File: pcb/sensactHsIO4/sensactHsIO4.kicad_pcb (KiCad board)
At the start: 2 copper layers, 90 x 58.5 mm, 148 parts, among them J1 Bus, J2 PROG, J3 OUT0-3, J4 IN0-3 IO4-7, J5 IO8-15, J6 PSU+BUS, J7 L- L+ R- R+, Q1 IRLML6344, Q10 IRLML6344, Q11 IRLML6344, Q12 IRLML6344, Q2 IRLML6344, Q3 IRLML6344, Q4 IRLML6344, Q5 IRLML6344, Q6 IRLML6344, Q7 IRLML6344, Q8 IRLML6344, Q9 IRLML6344, SW1 BOOT, SW2 TERM OFF ON, U1 ESP32-WROOM-32U, U10 SRV05, U11 SRV05, U12 SRV05, U13 MAX98357AETE+T, U14 MAX98357AETE+T, U2 SN65HVD230, U3 MAX3485, U4 CPC1018N, U5 CPC1018N, U6 CPC1018N, U7 CPC1018N, U8 LMR14206, U9 SRV05

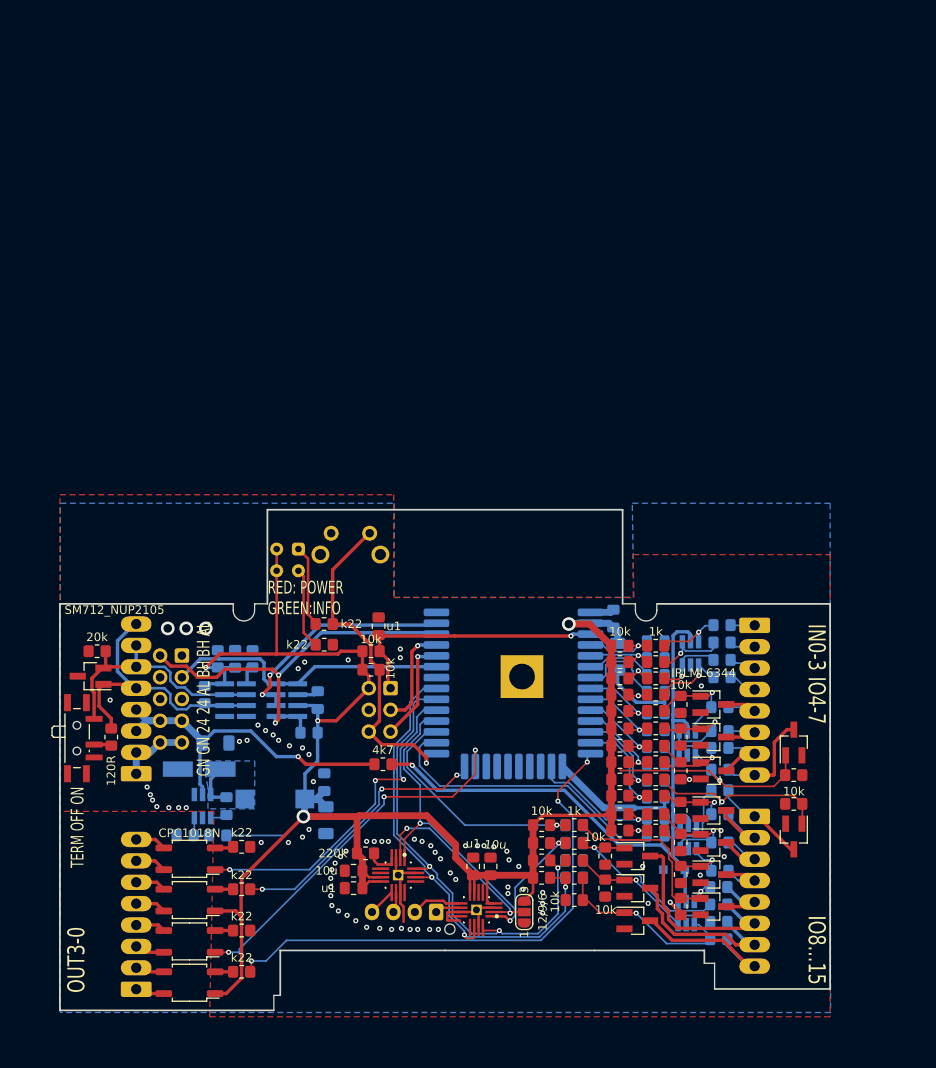
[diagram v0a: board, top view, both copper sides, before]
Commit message: Improvements in pcb design of sensactOutdoor and sensactHsIO4
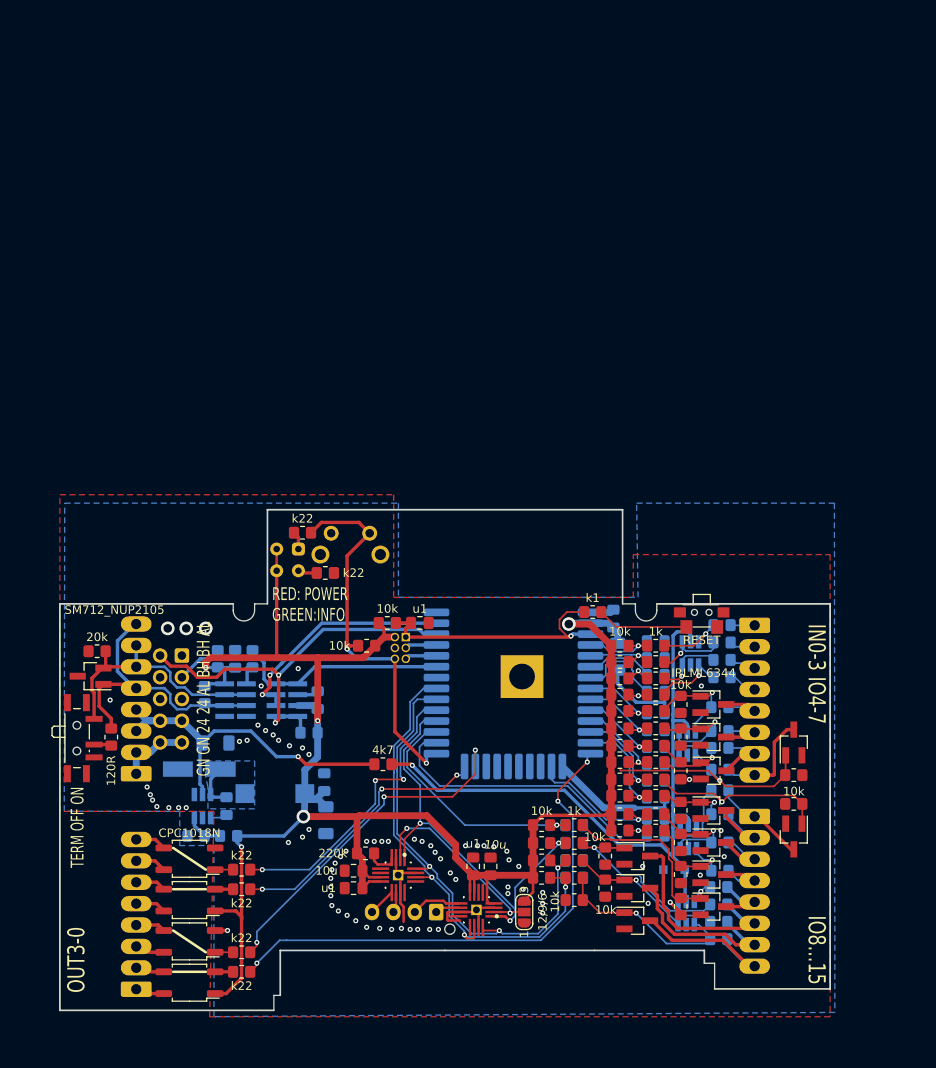
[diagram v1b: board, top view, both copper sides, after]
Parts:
- added R79: k1, Resistor_SMD:R_0805_2012Metric_Pad1.20x1.40mm_HandSolder, F.Cu at (167.3, 108.7)
- added SW3: RESET, sensact:SW_SPST_2x4x3,5, F.Cu at (180.0, 108.8)
- J2: footprint Connector_IDC:IDC-Header_2x03_P2.54mm_Vertical -> liebler_CONN:IDC_2x03_P1.27mm_Vertical
- moved R3 11.0 mm to (133.3, 99.4)
- moved R77 8.38 mm to (136.0, 104.1)
- moved C1 4.84 mm to (147.1, 110.0), turned to 180 degrees
- moved J2 4.84 mm to (144.8, 112.9)
- moved R1 3.81 mm to (143.3, 110.0)
- moved R2 2.84 mm to (140.8, 112.6), turned to 0 degrees
- moved R8 2.67 mm to (126.2, 138.8)
- moved R6 2.54 mm to (126.2, 148.5)
- moved R10 1.27 mm to (120.9, 134.9)
- moved R9 1.27 mm to (124.7, 134.9)
- moved L1 0.64 mm to (130.1, 129.9)
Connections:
- R6 pad 1: GND -> OUT2
- R8 pad 1: GND -> OUT0
- U5 pad 1: OUT2 -> Net-(R6-Pad2)
- U5 pad 2: Net-(R6-Pad2) -> GND
- U7 pad 1: OUT0 -> Net-(R8-Pad2)
- U7 pad 2: Net-(R8-Pad2) -> GND
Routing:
- net Net-(R79-Pad1): track 0.00 -> 10.7 mm
- net PROG_RX: track 12.3 -> 3.73 mm, vias 1 -> 0
- net PROG_TX: track 12.0 -> 3.73 mm, vias 1 -> 0
- net Net-(D1-Pad1): track 9.59 -> 2.12 mm
- net Net-(D1-Pad3): track 9.47 -> 2.25 mm
- net PROG_IO0: track 39.8 -> 46.0 mm, vias 1 -> 2
- net OUT0: track 38.8 -> 34.7 mm
- net OUT2: track 44.5 -> 41.1 mm
- net +3V3: track 218.5 -> 217.0 mm, vias 4 -> 5
- net GND: track 70.1 -> 71.6 mm, vias 81 -> 77
- net /psu/FB: track 3.92 -> 4.44 mm
- net OUT3: track 61.8 -> 61.3 mm

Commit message: various changes
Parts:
- added C30: 1u, Capacitor_SMD:C_1206_3216Metric_Pad1.33x1.80mm_HandSolder, F.Cu at (120.8, 124.0)
- added C31: 1u, Capacitor_SMD:C_0805_2012Metric_Pad1.18x1.45mm_HandSolder, F.Cu at (139.4, 135.9)
- added J11: BUS, Connector_Phoenix_MC:PhoenixContact_MC_1,5_4-G-3.5_1x04_P3.50mm_Horizontal, B.Cu at (113.0, 120.8)
- added J12: 24V, Connector_Phoenix_MC:PhoenixContact_MC_1,5_2-G-3.5_1x02_P3.50mm_Horizontal, B.Cu at (113.0, 130.0)
- added R80: 4k7, Resistor_SMD:R_0805_2012Metric_Pad1.20x1.40mm_HandSolder, F.Cu at (149.4, 132.8)
- added R81: 4k7, Resistor_SMD:R_0805_2012Metric_Pad1.20x1.40mm_HandSolder, F.Cu at (137.5, 140.8)
- added R82: 4k7, Resistor_SMD:R_0805_2012Metric_Pad1.20x1.40mm_HandSolder, F.Cu at (135.5, 140.8)
- added R83: 4k7, Resistor_SMD:R_0805_2012Metric_Pad1.20x1.40mm_HandSolder, F.Cu at (133.5, 140.8)
- added R84: 4k7, Resistor_SMD:R_0805_2012Metric_Pad1.20x1.40mm_HandSolder, F.Cu at (131.4, 140.8)
- added R85: 2k2, Resistor_SMD:R_0805_2012Metric_Pad1.20x1.40mm_HandSolder, F.Cu at (139.6, 140.8)
- added R86: 2k2, Resistor_SMD:R_0805_2012Metric_Pad1.20x1.40mm_HandSolder, F.Cu at (139.3, 137.9)
- added R87: 2k2, Resistor_SMD:R_0805_2012Metric_Pad1.20x1.40mm_HandSolder, F.Cu at (130.4, 137.0)
- added R88: 2k2, Resistor_SMD:R_0805_2012Metric_Pad1.20x1.40mm_HandSolder, F.Cu at (129.4, 140.8)
- added SW4: INT0, liebler_MECH:SS12D00, B.Cu at (135.5, 107.1)
- added SW5: INT1, liebler_MECH:SS12D00, B.Cu at (135.5, 121.0)
- added SW6: INT2, liebler_MECH:SS12D00, B.Cu at (135.5, 117.3)
- C4: value u1 -> 10u; footprint Capacitor_SMD:C_0805_2012Metric_Pad1.18x1.45mm_HandSolder -> Capacitor_SMD:C_1206_3216Metric_Pad1.33x1.80mm_HandSolder
- D3: value SM712_NUP2105 -> NUP2105
- J6: value PSU+BUS -> AIN; footprint liebler_CONN:PhoenixContact_MC_0,5_8-G-2.5_1x08_P2.50mm_Horizontal -> Connector_JST:JST_XH_B4B-XH-AM_1x04_P2.50mm_Vertical
- R4: value 10k -> isI2C; footprint Resistor_SMD:R_0805_2012Metric_Pad1.20x1.40mm_HandSolder -> Resistor_SMD:R_1206_3216Metric_Pad1.30x1.75mm_HandSolder
- R71: value 20k -> isI2C; footprint Resistor_SMD:R_0805_2012Metric_Pad1.20x1.40mm_HandSolder -> Resistor_SMD:R_1206_3216Metric_Pad1.30x1.75mm_HandSolder; moved to B.Cu
- R72: value 20k -> 4k7; moved to F.Cu
- R75, R76: footprint Resistor_SMD:R_0805_2012Metric_Pad1.20x1.40mm_HandSolder -> Resistor_SMD:R_1206_3216Metric_Pad1.30x1.75mm_HandSolder
- U2: value SN65HVD230 -> ISO1050DUB; footprint sensact:SOIC-8_3.9x4.9mm_Pitch1.27mm_handsolder -> liebler_SEMICONDUCTORS:SOP-8_6.62x9.15mm_P2.54mm_handsolder
- U3: value MAX3485 -> ADS1115IDGS; footprint sensact:SOIC-8_3.9x4.9mm_Pitch1.27mm_handsolder -> Package_SO:TSSOP-10_3x3mm_P0.5mm; moved to F.Cu
- moved J6 29.1 mm to (138.2, 143.8), turned to 180 degrees
- moved R71 26.4 mm to (135.8, 113.4), turned to 0 degrees
- moved R72 23.2 mm to (140.8, 131.8)
- moved U3 19.4 mm to (134.5, 137.0), turned to 0 degrees
- moved R74 19.4 mm to (123.8, 122.4)
- moved R76 19.3 mm to (119.0, 110.7), turned to 90 degrees
- moved R10 18.8 mm to (139.4, 131.6), turned to 0 degrees
- moved C5 18.0 mm to (141.7, 106.4), turned to 0 degrees
- moved R9 15.7 mm to (139.4, 129.5), turned to 0 degrees
- moved U2 9.09 mm to (135.8, 112.1)
- moved R4 8.89 mm to (135.8, 110.9), turned to 0 degrees
- moved C4 8.75 mm to (128.4, 113.4), turned to 270 degrees
- moved C8 8.30 mm to (140.5, 126.0), turned to 90 degrees
- moved R75 7.67 mm to (116.6, 110.7), turned to 90 degrees
- moved R2 6.53 mm to (143.5, 118.6), turned to 180 degrees
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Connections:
- C4 pad 1: +3V3 -> +5VA
- C4 pad 2: GND -> GNDA
- D3 pad 1: RS485_A -> CANL
- D3 pad 2: RS485_B -> CANH
- D3 pad 3: GND -> GNDA
- J1 pad 2: SCL -> CANH
- J1 pad 3: SDA -> CANL
- J1 pad 4: Net-(J1-Pad4) -> +5VA
- J1 pad 6: Net-(J1-Pad6) -> GNDA
- J6 pad 1: GND -> Net-(J6-Pad1)
- J6 pad 2: GND -> Net-(J6-Pad2)
- J6 pad 3: +24V -> Net-(J6-Pad3)
- J6 pad 4: +24V -> Net-(J6-Pad4)
- R4 pad 1: GND -> CANH
- R4 pad 2: Net-(R4-Pad2) -> CANR
- R71 pad 1: RS485_B -> CANL
- R71 pad 2: GND -> CANT
- R72 pad 1: +3V3 -> IO15
- R72 pad 2: RS485_A -> +3V3
- R73 pad 1: RS485_A -> CANH
- R75 pad 1: SDA -> CANH
- R76 pad 1: SCL -> CANL
- SW2 pad 1: RS485_B -> CANL
- U1 pad 33: SDA -> CANT
- U1 pad 36: SCL -> CANR
- U1 pad 37: DE_RE -> IRQ
- U2 pad 1: SDA -> +3V3
- U2 pad 2: GND -> CANR
- U2 pad 3: +3V3 -> CANT
- U2 pad 4: SCL -> GND
- U2 pad 5: Net-(U2-Pad5) -> GNDA
- U2 pad 6: RS485_A -> CANL
- U2 pad 7: RS485_B -> CANH
- U2 pad 8: Net-(R4-Pad2) -> +5VA
- U3 pad 1: SDA -> GND
- U3 pad 2: DE_RE -> Net-(U3-Pad2)
- U3 pad 3: DE_RE -> GND
- U3 pad 4: SCL -> Net-(R83-Pad2)
- U3 pad 5: GND -> Net-(R84-Pad2)
- U3 pad 6: RS485_A -> Net-(R81-Pad2)
- U3 pad 7: RS485_B -> Net-(R82-Pad2)
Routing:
- net CANH: track 0.00 -> 52.4 mm
- net SCL: track 50.3 -> 0.00 mm, vias 2 -> 0
- net CANL: track 0.00 -> 41.9 mm, vias 0 -> 1
- net RS485_A: track 36.6 -> 0.00 mm
- net SDA: track 34.9 -> 0.00 mm
- net GNDA: track 0.00 -> 32.4 mm
- net +5VA: track 0.00 -> 30.4 mm
- net RS485_B: track 30.0 -> 0.00 mm
- net DE_RE: track 27.7 -> 0.00 mm, vias 2 -> 0
- net IRQ: track 0.00 -> 27.0 mm
- net 3V3_ZDIODE: track 77.9 -> 98.9 mm
- net +3V3: track 217.0 -> 237.9 mm
- net Net-(J1-Pad5): track 0.00 -> 17.4 mm
- net /psu/FB: track 4.44 -> 21.8 mm
- net IO15: track 62.0 -> 78.5 mm, vias 3 -> 6
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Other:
- rule pad_to_mask_clearance: 0.05 -> 0
- board text added: "CH CL CL CH"
- board text added: "GN 24"
- board text removed: "GN GN 24 24 AL BH BH AL"

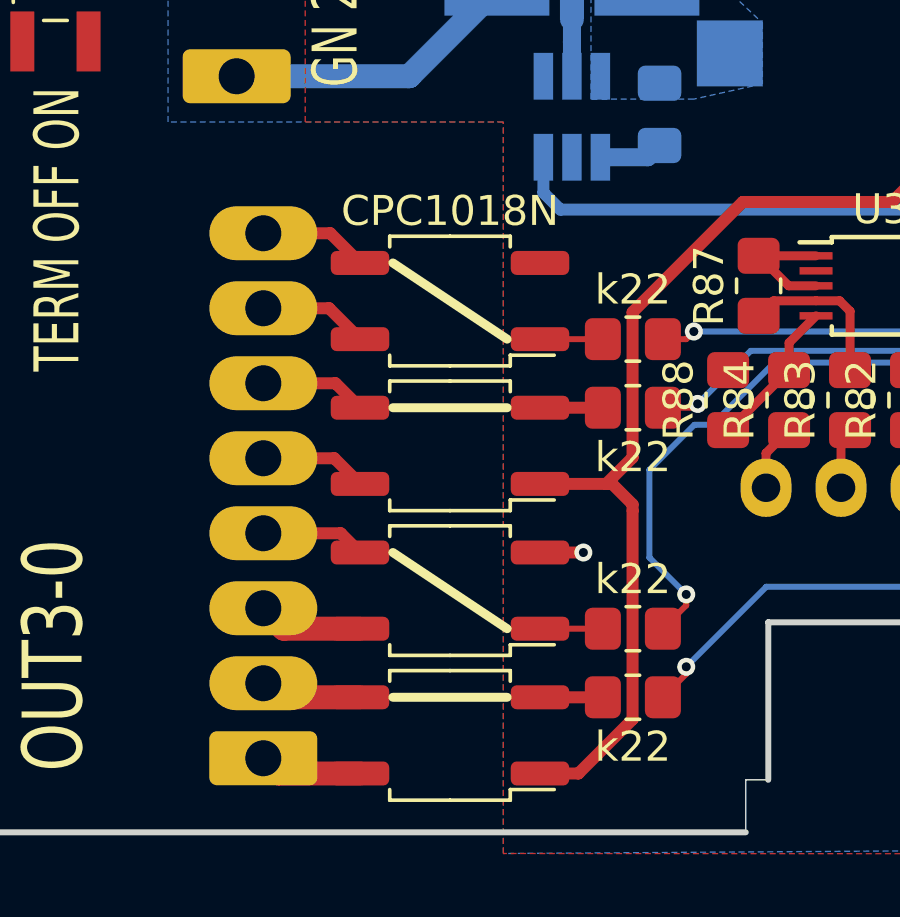
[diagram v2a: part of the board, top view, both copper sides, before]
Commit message: Renamed liebler_IC to liebler_SEMICONDUCTORS
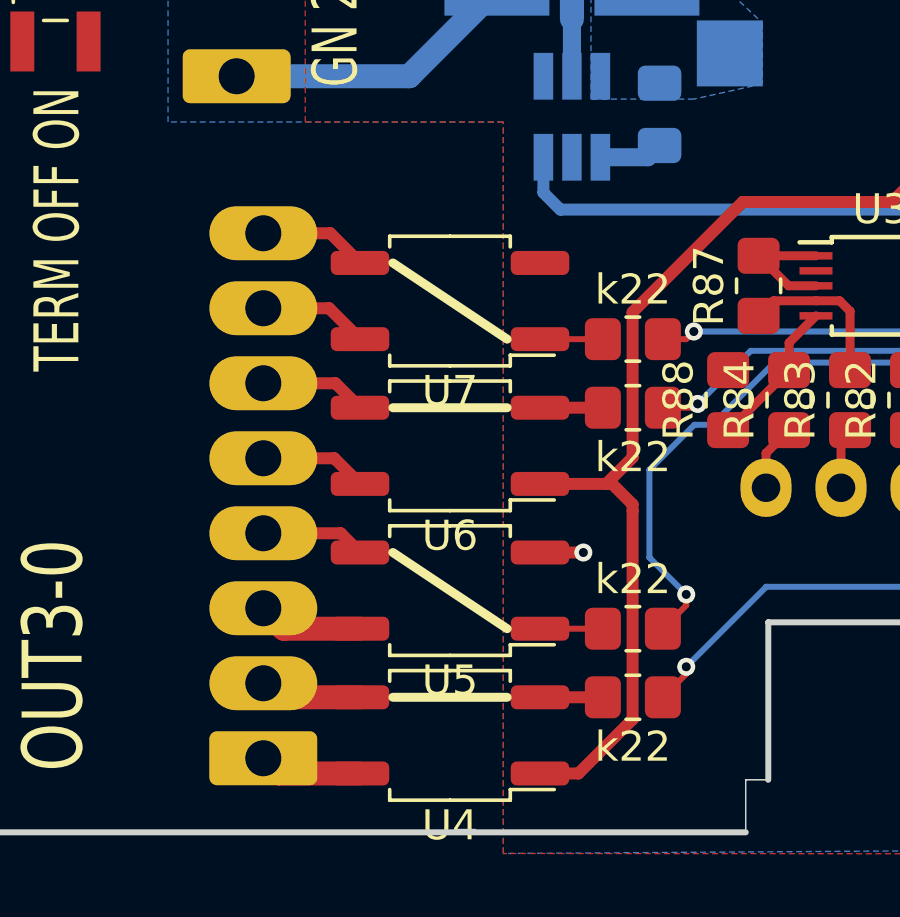
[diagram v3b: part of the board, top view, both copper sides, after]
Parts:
- U4, U5, U6, U7: footprint liebler_IC:SOP-4_3.8x4.1mm_P2.54mm_handsolder -> liebler_SEMICONDUCTORS:SOP-4_3.8x4.1mm_P2.54mm_handsolder

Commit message: PCB optimizations
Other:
- outline, holes or cut-outs redrawn

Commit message: Various
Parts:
- removed C28: 10u, Capacitor_SMD:C_0805_2012Metric_Pad1.18x1.45mm_HandSolder
- removed C29: u1, Capacitor_SMD:C_0805_2012Metric_Pad1.18x1.45mm_HandSolder
- removed C30: 1u, Capacitor_SMD:C_1206_3216Metric_Pad1.33x1.80mm_HandSolder
- removed C31: 1u, Capacitor_SMD:C_0805_2012Metric_Pad1.18x1.45mm_HandSolder
- removed J11: BUS, Connector_Phoenix_MC:PhoenixContact_MC_1,5_4-G-3.5_1x04_P3.50mm_Horizontal
- removed J12: 24V, Connector_Phoenix_MC:PhoenixContact_MC_1,5_2-G-3.5_1x02_P3.50mm_Horizontal
- removed Q10, Q11, Q12, Q3, Q4, Q5, Q6, Q7, Q8, Q9: IRLML6344, Package_TO_SOT_SMD:SOT-23_Handsoldering
- removed R80, R81, R82, R83, R84: 4k7, Resistor_SMD:R_0805_2012Metric_Pad1.20x1.40mm_HandSolder
- removed R85, R86, R87, R88: 2k2, Resistor_SMD:R_0805_2012Metric_Pad1.20x1.40mm_HandSolder
- removed SW1: BOOT, Button_Switch_THT:SW_Tactile_SPST_Angled_PTS645Vx58-2LFS
- added BZ1: Buzzer, liebler_MECH:XDCR_CMT-7525-80-SMT-TR, B.Cu at (137.5, 85.4)
- added D5: NUP2105L, Package_TO_SOT_SMD:SOT-23_Handsoldering, B.Cu at (181.8, 138.6)
- added H1: MountingHole, MountingHole:MountingHole_2mm, F.Cu at (169.0, 43.4)
- added H2: MountingHole, MountingHole:MountingHole_2mm, F.Cu at (159.5, 58.5)
- added J8: Conn_01x10, Connector_FFC-FPC:Hirose_FH12-10S-0.5SH_1x10-1MP_P0.50mm_Horizontal, B.Cu at (147.8, 86.8)
- added J9: AOUT, Connector_JST:JST_XH_B4B-XH-A_1x04_P2.50mm_Vertical, B.Cu at (151.5, 137.7)
- added JP10: OUT_IN0, Jumper:SolderJumper-3_P1.3mm_Open_RoundedPad1.0x1.5mm, F.Cu at (118.3, 120.4)
- added JP11: OUT_IN0, Jumper:SolderJumper-3_P1.3mm_Open_RoundedPad1.0x1.5mm, F.Cu at (118.3, 126.6)
- added JP12: OUT_IN0, Jumper:SolderJumper-3_P1.3mm_Open_RoundedPad1.0x1.5mm, F.Cu at (118.3, 134.4)
- added JP13: OUT_IN0, Jumper:SolderJumper-3_P1.3mm_Open_RoundedPad1.0x1.5mm, F.Cu at (122.9, 114.2)
- added JP14: OUT_IN0, Jumper:SolderJumper-3_P1.3mm_Open_RoundedPad1.0x1.5mm, F.Cu at (122.9, 120.4)
- added JP15: OUT_IN0, Jumper:SolderJumper-3_P1.3mm_Open_RoundedPad1.0x1.5mm, F.Cu at (122.9, 126.6)
- added JP16: OUT_IN0, Jumper:SolderJumper-3_P1.3mm_Open_RoundedPad1.0x1.5mm, F.Cu at (122.9, 134.4)
- added JP17: OUT_IN0, Jumper:SolderJumper-3_P1.3mm_Open_RoundedPad1.0x1.5mm, F.Cu at (118.3, 137.5)
- added JP18: OUT_IN0, Jumper:SolderJumper-3_P1.3mm_Open_RoundedPad1.0x1.5mm, F.Cu at (118.3, 143.7)
- added JP19: OUT_IN0, Jumper:SolderJumper-3_P1.3mm_Open_RoundedPad1.0x1.5mm, F.Cu at (118.3, 149.9)
- added JP2: OUT_IN0, Jumper:SolderJumper-3_P1.3mm_Open_RoundedPad1.0x1.5mm, F.Cu at (118.3, 117.3)
- added JP20: OUT_IN0, Jumper:SolderJumper-3_P1.3mm_Open_RoundedPad1.0x1.5mm, F.Cu at (122.9, 137.5)
- added JP21: OUT_IN0, Jumper:SolderJumper-3_P1.3mm_Open_RoundedPad1.0x1.5mm, F.Cu at (122.9, 143.7)
- added JP22: OUT_IN0, Jumper:SolderJumper-3_P1.3mm_Open_RoundedPad1.0x1.5mm, F.Cu at (122.9, 149.9)
- added JP23: OUT_IN0, Jumper:SolderJumper-3_P1.3mm_Open_RoundedPad1.0x1.5mm, F.Cu at (118.3, 140.6)
- added JP24: OUT_IN0, Jumper:SolderJumper-3_P1.3mm_Open_RoundedPad1.0x1.5mm, F.Cu at (118.3, 146.8)
- added JP25: OUT_IN0, Jumper:SolderJumper-3_P1.3mm_Open_RoundedPad1.0x1.5mm, F.Cu at (118.3, 153.0)
- added JP26: OUT_IN0, Jumper:SolderJumper-3_P1.3mm_Open_RoundedPad1.0x1.5mm, F.Cu at (122.9, 140.6)
- added JP27: OUT_IN0, Jumper:SolderJumper-3_P1.3mm_Open_RoundedPad1.0x1.5mm, F.Cu at (122.9, 146.8)
- added JP28: OUT_IN0, Jumper:SolderJumper-3_P1.3mm_Open_RoundedPad1.0x1.5mm, F.Cu at (123.0, 152.9)
- added JP29: SCL, Jumper:SolderJumper-2_P1.3mm_Open_RoundedPad1.0x1.5mm, F.Cu at (169.7, 126.8)
- added JP3: OUT_IN0, Jumper:SolderJumper-3_P1.3mm_Open_RoundedPad1.0x1.5mm, F.Cu at (118.3, 123.5)
- added JP30: SDA, Jumper:SolderJumper-2_P1.3mm_Open_RoundedPad1.0x1.5mm, F.Cu at (169.7, 124.2)
- added JP31: IO12, Jumper:SolderJumper-3_P1.3mm_Open_RoundedPad1.0x1.5mm, F.Cu at (163.4, 128.1)
- added JP32: BUST, Jumper:SolderJumper-3_P1.3mm_Open_RoundedPad1.0x1.5mm, F.Cu at (166.8, 140.6)
- added JP33: BUSR, Jumper:SolderJumper-3_P1.3mm_Open_RoundedPad1.0x1.5mm, F.Cu at (166.8, 136.8)
- added JP34: BUST, Jumper:SolderJumper-3_P1.3mm_Open_RoundedPad1.0x1.5mm, F.Cu at (183.5, 143.6)
- added JP35: BUSR, Jumper:SolderJumper-3_P1.3mm_Open_RoundedPad1.0x1.5mm, F.Cu at (183.5, 138.8)
- added JP4: OUT_IN0, Jumper:SolderJumper-3_P1.3mm_Open_RoundedPad1.0x1.5mm, F.Cu at (118.3, 129.7)
- added JP5: OUT_IN0, Jumper:SolderJumper-3_P1.3mm_Open_RoundedPad1.0x1.5mm, F.Cu at (122.9, 111.1)
- added JP6: OUT_IN0, Jumper:SolderJumper-3_P1.3mm_Open_RoundedPad1.0x1.5mm, F.Cu at (122.9, 117.3)
- added JP7: OUT_IN0, Jumper:SolderJumper-3_P1.3mm_Open_RoundedPad1.0x1.5mm, F.Cu at (122.9, 123.5)
- added JP8: OUT_IN0, Jumper:SolderJumper-3_P1.3mm_Open_RoundedPad1.0x1.5mm, F.Cu at (122.9, 129.7)
- added JP9: OUT_IN0, Jumper:SolderJumper-3_P1.3mm_Open_RoundedPad1.0x1.5mm, F.Cu at (118.3, 114.2)
- added U15: SRV05-4, liebler_SEMICONDUCTORS:SOT-23-6-spezial, B.Cu at (149.4, 132.8)
- added U16: SRV05-4, liebler_SEMICONDUCTORS:SOT-23-6-spezial, B.Cu at (158.9, 132.8)
- added X1: LH114, liebler_OPTO:FP-114 13pol, F.Cu at (149.0, 90.0)
- C1, C27: footprint Capacitor_SMD:C_0805_2012Metric_Pad1.18x1.45mm_HandSolder -> Capacitor_SMD:C_0402_1005Metric; moved to B.Cu
- C10, C11, C12, C13, C14, C15, C16, C17, C18, C19, C2, C20, C22, C7, C9: footprint Capacitor_SMD:C_0805_2012Metric_Pad1.18x1.45mm_HandSolder -> Capacitor_SMD:C_0603_1608Metric
- C21: value u1 -> 10u; footprint Capacitor_SMD:C_0805_2012Metric_Pad1.18x1.45mm_HandSolder -> Capacitor_SMD:C_1206_3216Metric
- C23: value u1 -> 10n; footprint Capacitor_SMD:C_0805_2012Metric_Pad1.18x1.45mm_HandSolder -> Capacitor_SMD:C_0603_1608Metric
- C24: value u1 -> 22u; footprint Capacitor_SMD:C_0805_2012Metric_Pad1.18x1.45mm_HandSolder -> Capacitor_SMD:C_0603_1608Metric
- C25, C5: footprint Capacitor_SMD:C_0805_2012Metric_Pad1.18x1.45mm_HandSolder -> Capacitor_SMD:C_0402_1005Metric
- C26: value 10u -> 1u; footprint Capacitor_SMD:C_0805_2012Metric_Pad1.18x1.45mm_HandSolder -> Capacitor_SMD:C_0402_1005Metric; moved to B.Cu
- C3: value 22u -> u1; footprint Capacitor_SMD:C_1206_3216Metric_Pad1.33x1.80mm_HandSolder -> Capacitor_SMD:C_0603_1608Metric
- C4: value 10u -> u1; footprint Capacitor_SMD:C_1206_3216Metric_Pad1.33x1.80mm_HandSolder -> Capacitor_SMD:C_0402_1005Metric
- C6: value 4u7 -> 22u; footprint Capacitor_SMD:C_1206_3216Metric_Pad1.33x1.80mm_HandSolder -> Capacitor_SMD:C_0603_1608Metric
- C8: value m1 -> u1; footprint Capacitor_SMD:C_1206_3216Metric_Pad1.33x1.80mm_HandSolder -> Capacitor_SMD:C_0603_1608Metric
- D1: value R_POWER_G_INFO -> SM712; footprint liebler_SEMICONDUCTORS:Dialight-5530123F-0 -> Package_TO_SOT_SMD:SOT-23_Handsoldering
- D2: value MBR0540 -> D; footprint Diode_SMD:D_SMA_Handsoldering -> Diode_SMD:D_SOD-123
- D3: value NUP2105 -> 3V; footprint Package_TO_SOT_SMD:SOT-23_Handsoldering -> Diode_SMD:D_SOD-123; moved to B.Cu
- D4: value 3V -> SS34; footprint Diode_SMD:D_SOD-323_HandSoldering -> Diode_SMD:D_SMA
- J1: value Bus -> BUS; footprint Connector_IDC:IDC-Header_2x05_P2.54mm_Horizontal -> Connector_Phoenix_MC:PhoenixContact_MC_1,5_4-G-3.5_1x04_P3.50mm_Horizontal
- J2: value PROG -> Bus; footprint liebler_CONN:IDC_2x03_P1.27mm_Vertical -> Connector_IDC:IDC-Header_2x05_P2.54mm_Horizontal
- J3: value OUT0-3 -> 24V; footprint liebler_CONN:PhoenixContact_MC_0,5_8-G-2.5_1x08_P2.50mm_Horizontal -> Connector_Phoenix_MC:PhoenixContact_MC_1,5_2-G-3.5_1x02_P3.50mm_Horizontal
- J4: value IN0-3 IO4-7 -> PROG; footprint liebler_CONN:PhoenixContact_MC_0,5_8-G-2.5_1x08_P2.50mm_Horizontal -> liebler_CONN:IDC_2x03_P1.27mm_Vertical
- J5: value IO8-15 -> IN0-3 IO4-7
- J6: value AIN -> IO8-15; footprint Connector_JST:JST_XH_B4B-XH-AM_1x04_P2.50mm_Vertical -> liebler_CONN:PhoenixContact_MC_0,5_8-G-2.5_1x08_P2.50mm_Horizontal
- J7: value L- L+ R- R+ -> HMI; footprint Connector_JST:JST_XH_B4B-XH-AM_1x04_P2.50mm_Vertical -> Connector_FFC-FPC:Hirose_FH12-10S-0.5SH_1x10-1MP_P0.50mm_Horizontal
- JP1: value 12/9/6 -> OUT_IN0; footprint Jumper:SolderJumper-3_P1.3mm_Open_RoundedPad1.0x1.5mm_NumberLabels -> Jumper:SolderJumper-3_P1.3mm_Open_RoundedPad1.0x1.5mm
- L1: value 33u -> 6u8; footprint sensact:L_7.3x7.3_H4.5_handsolder -> Inductor_SMD:L_Abracon_ASPI-0630LR
- Q1, Q2: value IRLML6344 -> AO3400A; footprint Package_TO_SOT_SMD:SOT-23_Handsoldering -> Package_TO_SOT_SMD:SOT-23; moved to B.Cu
- R1, R19, R28, R29, R30: value 10k -> k1; footprint Resistor_SMD:R_0805_2012Metric_Pad1.20x1.40mm_HandSolder -> Resistor_SMD:R_0603_1608Metric; moved to B.Cu
- R10: value 1k -> 10k; footprint Resistor_SMD:R_0805_2012Metric_Pad1.20x1.40mm_HandSolder -> Resistor_SMD:R_0402_1005Metric
- R11: value 10R -> 4k7; footprint Resistor_SMD:R_0805_2012Metric_Pad1.20x1.40mm_HandSolder -> Resistor_SMD:R_0603_1608Metric
- R12, R13, R14, R24, R25, R26: footprint Resistor_SMD:R_0805_2012Metric_Pad1.20x1.40mm_HandSolder -> Resistor_SMD:R_0603_1608Metric
- R15, R47, R66: value 1k -> 10R; footprint Resistor_SMD:R_0805_2012Metric_Pad1.20x1.40mm_HandSolder -> Resistor_SMD:R_0603_1608Metric; moved to B.Cu
- R16, R17, R18, R31, R48, R49, R50: value 1k -> k1; footprint Resistor_SMD:R_0805_2012Metric_Pad1.20x1.40mm_HandSolder -> Resistor_SMD:R_0603_1608Metric; moved to B.Cu
- R2, R20, R21, R22, R35, R43, R44, R51, R52, R53: footprint Resistor_SMD:R_0805_2012Metric_Pad1.20x1.40mm_HandSolder -> Resistor_SMD:R_0603_1608Metric; moved to B.Cu
- R23, R42: value 10R -> 10k; footprint Resistor_SMD:R_0805_2012Metric_Pad1.20x1.40mm_HandSolder -> Resistor_SMD:R_0603_1608Metric
- R27, R36, R37, R38, R45, R46, R67, R68, R69, R70: value 10k -> 10R; footprint Resistor_SMD:R_0805_2012Metric_Pad1.20x1.40mm_HandSolder -> Resistor_SMD:R_0603_1608Metric; moved to B.Cu
- R3: value k22 -> 10k; footprint Resistor_SMD:R_0805_2012Metric_Pad1.20x1.40mm_HandSolder -> Resistor_SMD:R_0603_1608Metric; moved to B.Cu
- R32, R33, R34: value 1k -> 10k; footprint Resistor_SMD:R_0805_2012Metric_Pad1.20x1.40mm_HandSolder -> Resistor_SMD:R_0603_1608Metric; moved to B.Cu
- R39, R40, R41: value 10R -> k1; footprint Resistor_SMD:R_0805_2012Metric_Pad1.20x1.40mm_HandSolder -> Resistor_SMD:R_0603_1608Metric
- R4: value isI2C -> 1k; footprint Resistor_SMD:R_1206_3216Metric_Pad1.30x1.75mm_HandSolder -> Resistor_SMD:R_0402_1005Metric
- R5, R6: value k22 -> 1k; footprint Resistor_SMD:R_0805_2012Metric_Pad1.20x1.40mm_HandSolder -> Resistor_SMD:R_0603_1608Metric; moved to B.Cu
- R54: value 10k -> 75k; footprint Resistor_SMD:R_0805_2012Metric_Pad1.20x1.40mm_HandSolder -> Resistor_SMD:R_0603_1608Metric; moved to B.Cu
- R55: value 10R -> 24K; footprint Resistor_SMD:R_0805_2012Metric_Pad1.20x1.40mm_HandSolder -> Resistor_SMD:R_0603_1608Metric
- R56, R58: value 10R -> 1k; footprint Resistor_SMD:R_0805_2012Metric_Pad1.20x1.40mm_HandSolder -> Resistor_SMD:R_0402_1005Metric
- R57: value 10R -> 1k; footprint Resistor_SMD:R_0805_2012Metric_Pad1.20x1.40mm_HandSolder -> Resistor_SMD:R_0603_1608Metric
- R59: value 10k -> 4k7; footprint Resistor_SMD:R_0805_2012Metric_Pad1.20x1.40mm_HandSolder -> Resistor_SMD:R_0402_1005Metric; moved to B.Cu
- R60: value 10k -> 3k3; footprint Resistor_SMD:R_0805_2012Metric_Pad1.20x1.40mm_HandSolder -> Resistor_SMD:R_0402_1005Metric; moved to B.Cu
- R61: value 10k -> 2k2; footprint Resistor_SMD:R_0805_2012Metric_Pad1.20x1.40mm_HandSolder -> Resistor_SMD:R_0402_1005Metric; moved to B.Cu
- R62: footprint Resistor_SMD:R_0805_2012Metric_Pad1.20x1.40mm_HandSolder -> Resistor_SMD:R_0402_1005Metric; moved to B.Cu
- R63: value 1k -> 22k; footprint Resistor_SMD:R_0805_2012Metric_Pad1.20x1.40mm_HandSolder -> Resistor_SMD:R_0402_1005Metric; moved to B.Cu
- R64: value 1k -> K24; footprint Resistor_SMD:R_0805_2012Metric_Pad1.20x1.40mm_HandSolder -> Resistor_SMD:R_0603_1608Metric; moved to B.Cu
- R65: value 1k -> 2K7; footprint Resistor_SMD:R_0805_2012Metric_Pad1.20x1.40mm_HandSolder -> Resistor_SMD:R_0603_1608Metric; moved to B.Cu
- R7: value k22 -> 10k; footprint Resistor_SMD:R_0805_2012Metric_Pad1.20x1.40mm_HandSolder -> Resistor_SMD:R_0402_1005Metric; moved to B.Cu
- R71: value isI2C -> 10R; footprint Resistor_SMD:R_1206_3216Metric_Pad1.30x1.75mm_HandSolder -> Resistor_SMD:R_0603_1608Metric
- R72, R74: value 4k7 -> 10R; footprint Resistor_SMD:R_0805_2012Metric_Pad1.20x1.40mm_HandSolder -> Resistor_SMD:R_0603_1608Metric; moved to B.Cu
- R73: value 120R -> 10R; footprint Resistor_SMD:R_0805_2012Metric_Pad1.20x1.40mm_HandSolder -> Resistor_SMD:R_0603_1608Metric; moved to B.Cu
- R75, R76: value 4k7 -> 10R; footprint Resistor_SMD:R_1206_3216Metric_Pad1.30x1.75mm_HandSolder -> Resistor_SMD:R_0603_1608Metric
- R77: value k22 -> 10R; footprint Resistor_SMD:R_0805_2012Metric_Pad1.20x1.40mm_HandSolder -> Resistor_SMD:R_0603_1608Metric; moved to B.Cu
- R78: value 220k -> 10R; footprint Resistor_SMD:R_0805_2012Metric_Pad1.20x1.40mm_HandSolder -> Resistor_SMD:R_0603_1608Metric; moved to B.Cu
- R79: value k1 -> 10R; footprint Resistor_SMD:R_0805_2012Metric_Pad1.20x1.40mm_HandSolder -> Resistor_SMD:R_0603_1608Metric; moved to B.Cu
- R8: value k22 -> k1; footprint Resistor_SMD:R_0805_2012Metric_Pad1.20x1.40mm_HandSolder -> Resistor_SMD:R_0603_1608Metric; moved to B.Cu
- R9: value 3k3 -> K12; footprint Resistor_SMD:R_0805_2012Metric_Pad1.20x1.40mm_HandSolder -> Resistor_SMD:R_0603_1608Metric
- SW2: value TERM OFF ON -> TERM ON
- SW3: value RESET -> Reset; footprint sensact:SW_SPST_2x4x3,5 -> liebler_MECH:Button_2x4x3,5_handsolder; moved to B.Cu
- SW4: value INT0 -> R; footprint liebler_MECH:SS12D00 -> liebler_MECH:Button_SMD_4,5x4,5; moved to F.Cu
- SW5: value INT1 -> L; footprint liebler_MECH:SS12D00 -> liebler_MECH:Button_SMD_4,5x4,5; moved to F.Cu
- SW6: value INT2 -> OK; footprint liebler_MECH:SS12D00 -> liebler_MECH:Button_SMD_4,5x4,5; moved to F.Cu
- U1: value ESP32-WROOM-32U -> ESP32-WROOM-32; footprint smopla:ESP32-WROOM-32_HANDSOLDER -> RF_Module:ESP32-WROOM-32
- U10: value SRV05 -> EUP3458; footprint Package_TO_SOT_SMD:SOT-23-6_Handsoldering -> Package_TO_SOT_SMD:SOT-23-6
- U11: value SRV05 -> LM317_TO-252; footprint Package_TO_SOT_SMD:SOT-23-6_Handsoldering -> Package_TO_SOT_SMD:TO-252-2
- U12: value SRV05 -> SP3485EN; footprint Package_TO_SOT_SMD:SOT-23-6_Handsoldering -> Package_SO:SOIC-8_3.9x4.9mm_P1.27mm
- U13, U14: value MAX98357AETE+T -> SRV05-4; footprint smopla:MAX98357AETE -> liebler_SEMICONDUCTORS:SOT-23-6-spezial; moved to B.Cu
- U2: value ISO1050DUB -> SN65HVD230; footprint liebler_SEMICONDUCTORS:SOP-8_6.62x9.15mm_P2.54mm_handsolder -> Package_SO:SOIC-8_3.9x4.9mm_P1.27mm
- U3: value ADS1115IDGS -> ULN2003; footprint Package_SO:TSSOP-10_3x3mm_P0.5mm -> Package_SO:SOP-16_3.9x9.9mm_P1.27mm; moved to B.Cu
- U4: value CPC1018N -> ULN2003; footprint liebler_SEMICONDUCTORS:SOP-4_3.8x4.1mm_P2.54mm_handsolder -> Package_SO:SOP-16_3.9x9.9mm_P1.27mm; moved to B.Cu
- U5: value CPC1018N -> LM358; footprint liebler_SEMICONDUCTORS:SOP-4_3.8x4.1mm_P2.54mm_handsolder -> Package_SO:SOIC-8_3.9x4.9mm_P1.27mm; moved to B.Cu
- U6, U7: value CPC1018N -> SRV05-4; footprint liebler_SEMICONDUCTORS:SOP-4_3.8x4.1mm_P2.54mm_handsolder -> liebler_SEMICONDUCTORS:SOT-23-6-spezial; moved to B.Cu
- U8: value LMR14206 -> SRV05-4; footprint Package_TO_SOT_SMD:SOT-23-6_Handsoldering -> liebler_SEMICONDUCTORS:SOT-23-6-spezial
- U9: value SRV05 -> SRV05-4; footprint Package_TO_SOT_SMD:SOT-23-6_Handsoldering -> liebler_SEMICONDUCTORS:SOT-23-6-spezial
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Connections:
- C1 pad 1: GND -> GND1
- C1 pad 2: PROG_EN -> /top_hmi/SW
- C10 pad 1: IN0 -> Net-(C10-Pad1)
- C11 pad 1: IN1 -> Net-(C11-Pad1)
- C12 pad 1: IN2 -> Net-(C12-Pad1)
- C13 pad 1: IN3 -> Net-(C13-Pad1)
- C14 pad 1: IO8 -> Net-(C14-Pad1)
- C15 pad 1: IO9 -> Net-(C15-Pad1)
- C16 pad 1: IO10 -> Net-(C16-Pad1)
- C17 pad 1: IO11 -> Net-(C17-Pad1)
- C18 pad 1: IO12 -> Net-(C18-Pad1)
- C19 pad 1: IO13 -> Net-(C19-Pad1)
- C2 pad 1: +3V3 -> PROG_EN
- C20 pad 1: IO14 -> Net-(C20-Pad1)
- C21 pad 1: IO15 -> GND
- C21 pad 2: GND -> +24V
- C22 pad 1: IO4 -> GND
- C22 pad 2: GND -> +24V
- C23 pad 1: IO5 -> Net-(C23-Pad1)
- C23 pad 2: GND -> /psu/SW
- C24 pad 1: IO6 -> +3V3
- C25 pad 1: IO7 -> GND
- C25 pad 2: GND -> +24V
- C26 pad 2: +3V3 -> +15V
- C4 pad 1: +5VA -> GND
- C4 pad 2: GNDA -> +15V
- C6 pad 1: +24V -> +3V3
- C7 pad 1: /psu/SW -> Net-(C7-Pad1)
- C7 pad 2: /psu/CB -> GND
- C8 pad 1: +3V3 -> Net-(C8-Pad1)
- C9 pad 1: +3V3 -> Net-(C9-Pad1)
- D1 pad 1: Net-(D1-Pad1) -> RS485B
- D1 pad 2: +3V3 -> RS485A
- D1 pad 3: Net-(D1-Pad3) -> GND
- D2 pad 1: /psu/SW -> Net-(D2-Pad1)
- D2 pad 2: GND -> +24V
- D3 pad 1: CANL -> +3V0
- D3 pad 2: CANH -> GND
- D4 pad 1: 3V3_ZDIODE -> /psu/SW
- J1 pad 1: Net-(J1-Pad1) -> BUS_2
- J1 pad 2: CANH -> BUS_1
- J1 pad 3: CANL -> BUS_1
- J1 pad 4: +5VA -> BUS_2
- J2 pad 1: PROG_EN -> unconnected-(J2-Pad1)
- J2 pad 2: +3V3 -> Net-(J2-Pad2)
- J2 pad 3: PROG_TX -> Net-(J2-Pad3)
- J2 pad 4: GND -> unconnected-(J2-Pad4)
- J2 pad 5: PROG_RX -> unconnected-(J2-Pad5)
- J2 pad 6: PROG_IO0 -> unconnected-(J2-Pad6)
- J3 pad 1: Net-(J3-Pad1) -> GND
- J3 pad 2: Net-(J3-Pad2) -> +24V
- J4 pad 1: /i4/OUT0 -> PROG_EN
- J4 pad 2: /i4/OUT1 -> +3V3
- J4 pad 3: /i4/OUT2 -> PROG_TX
- J4 pad 4: /i4/OUT3 -> GND
- J4 pad 5: /io4_A/OUT0 -> PROG_RX
- J4 pad 6: /io4_A/OUT1 -> BACKLIGHT
- J5 pad 1: /io4_B/OUT0 -> /CONN13
- J5 pad 2: /io4_B/OUT1 -> /CONN12
- J5 pad 3: /io4_B/OUT2 -> /CONN11
- J5 pad 4: /io4_B/OUT3 -> /CONN10
- J5 pad 5: /io4_C/OUT0 -> /CONN9
- J5 pad 6: /io4_C/OUT1 -> /CONN8
- J5 pad 7: /io4_C/OUT2 -> /CONN7
- J5 pad 8: /io4_C/OUT3 -> +24V
- J6 pad 1: Net-(J6-Pad1) -> /CONN6
- J6 pad 2: Net-(J6-Pad2) -> /CONN5
- J6 pad 3: Net-(J6-Pad3) -> /CONN4
- J6 pad 4: Net-(J6-Pad4) -> /CONN3
- J7 pad 1: /I2S_AMP/AUDIO_L_N -> BUZZER
- J7 pad 2: /I2S_AMP/AUDIO_L_P -> MOSI
- J7 pad 3: /I2S_AMP/AUDIO_R_N -> SCLK
- J7 pad 4: /I2S_AMP/AUDIO_R_P -> SW1
- JP1 pad 1: GND -> CPU0
- JP1 pad 2: Net-(JP1-Pad2) -> /CONN0
- JP1 pad 3: +3V3 -> Net-(JP1-Pad3)
- Q1 pad 1: /io4_B/S0 -> Net-(Q1-Pad1)
- Q1 pad 2: GND -> GND1
- Q1 pad 3: /io4_B/OUT0 -> Net-(Q1-Pad3)
- Q2 pad 1: /io4_B/S1 -> Net-(Q2-Pad1)
- Q2 pad 2: GND -> GND1
- Q2 pad 3: /io4_B/OUT1 -> Net-(Q2-Pad3)
- R1 pad 1: PROG_EN -> RESET
- R1 pad 2: +3V3 -> PROG_EN
- R10 pad 1: /psu/FB -> GND
- R10 pad 2: GND -> Net-(R10-Pad2)
- R11 pad 1: Net-(R11-Pad1) -> +3V0
- R11 pad 2: /i4/OUT0 -> Net-(D2-Pad1)
- R12 pad 1: Net-(R12-Pad1) -> /PROT0
- R12 pad 2: /i4/OUT1 -> Net-(JP1-Pad3)
- R13 pad 1: Net-(R13-Pad1) -> /PROT2
- R13 pad 2: /i4/OUT2 -> Net-(JP2-Pad3)
- R14 pad 1: Net-(R14-Pad1) -> /PROT4
- R14 pad 2: /i4/OUT3 -> Net-(JP3-Pad3)
- R15 pad 1: IN0 -> /PROT6
- R15 pad 2: Net-(R11-Pad1) -> Net-(JP4-Pad3)
- R16 pad 1: IN1 -> Net-(C7-Pad1)
- R16 pad 2: Net-(R12-Pad1) -> /PROT0
- R17 pad 1: IN2 -> Net-(C8-Pad1)
- R17 pad 2: Net-(R13-Pad1) -> /PROT2
- R18 pad 1: IN3 -> Net-(C9-Pad1)
- R18 pad 2: Net-(R14-Pad1) -> /PROT4
- R19 pad 1: IN0 -> Net-(C10-Pad1)
- R19 pad 2: +3V3 -> /PROT6
- R2 pad 1: PROG_IO0 -> PROG_EN
- R20 pad 1: IN1 -> Net-(C7-Pad1)
- R21 pad 1: IN2 -> Net-(C8-Pad1)
- R22 pad 1: IN3 -> Net-(C9-Pad1)
- R23 pad 1: /io4_B/S0 -> Net-(C10-Pad1)
- R23 pad 2: /io4_B/OUT0 -> +3V3
- R24 pad 1: /io4_B/S1 -> /PROT1
- R24 pad 2: /io4_B/OUT1 -> Net-(JP9-Pad3)
- R25 pad 1: Net-(Q3-Pad1) -> /PROT3
- R25 pad 2: /io4_B/OUT2 -> Net-(JP10-Pad3)
- R26 pad 1: Net-(Q4-Pad1) -> /PROT5
- R26 pad 2: /io4_B/OUT3 -> Net-(JP11-Pad3)
- R27 pad 1: GND -> /PROT7
- R27 pad 2: /io4_B/S0 -> Net-(JP12-Pad3)
- R28 pad 1: GND -> Net-(C11-Pad1)
- R28 pad 2: /io4_B/S1 -> /PROT1
- R29 pad 1: GND -> Net-(C12-Pad1)
- R29 pad 2: Net-(Q3-Pad1) -> /PROT3
- R3 pad 1: PROG_IO0 -> BACKLIGHT
- R3 pad 2: Net-(D1-Pad1) -> +3V3
- R30 pad 1: GND -> Net-(C13-Pad1)
- R30 pad 2: Net-(Q4-Pad1) -> /PROT5
- R31 pad 1: IO8 -> Net-(C14-Pad1)
- R31 pad 2: /io4_B/S0 -> /PROT7
- R32 pad 1: IO9 -> Net-(C11-Pad1)
- R32 pad 2: /io4_B/S1 -> +3V3
- R33 pad 1: IO10 -> Net-(C12-Pad1)
- R33 pad 2: Net-(Q3-Pad1) -> +3V3
- R34 pad 1: IO11 -> Net-(C13-Pad1)
- R34 pad 2: Net-(Q4-Pad1) -> +3V3
- R35 pad 1: IO8 -> Net-(C14-Pad1)
- R36 pad 1: IO9 -> /PROT8
- R36 pad 2: +3V3 -> Net-(JP17-Pad3)
- R37 pad 1: IO10 -> /PROT10
- R37 pad 2: +3V3 -> Net-(JP18-Pad3)
- R38 pad 1: IO11 -> /PROT12
- R38 pad 2: +3V3 -> Net-(JP19-Pad3)
- R39 pad 1: /io4_C/S0 -> Net-(C15-Pad1)
- R39 pad 2: /io4_C/OUT0 -> /PROT8
- R4 pad 1: CANH -> /top_hmi/BACKLIGHT
- R4 pad 2: CANR -> Net-(Q1-Pad1)
- R40 pad 1: /io4_C/S1 -> Net-(C16-Pad1)
- R40 pad 2: /io4_C/OUT1 -> /PROT10
- R41 pad 1: Net-(Q7-Pad1) -> Net-(C17-Pad1)
- R41 pad 2: /io4_C/OUT2 -> /PROT12
- R42 pad 1: Net-(Q8-Pad1) -> Net-(C15-Pad1)
- R42 pad 2: /io4_C/OUT3 -> +3V3
- R43 pad 1: GND -> Net-(C16-Pad1)
- R43 pad 2: /io4_C/S0 -> +3V3
- R44 pad 1: GND -> Net-(C17-Pad1)
- R44 pad 2: /io4_C/S1 -> +3V3
- R45 pad 1: GND -> /PROT9
- R45 pad 2: Net-(Q7-Pad1) -> Net-(JP23-Pad3)
- R46 pad 1: GND -> /PROT11
- R46 pad 2: Net-(Q8-Pad1) -> Net-(JP24-Pad3)
- R47 pad 1: IO12 -> /PROT13
- R47 pad 2: /io4_C/S0 -> Net-(JP25-Pad3)
- R48 pad 1: IO13 -> Net-(C18-Pad1)
- R48 pad 2: /io4_C/S1 -> /PROT9
- R49 pad 1: IO14 -> Net-(C19-Pad1)
- R49 pad 2: Net-(Q7-Pad1) -> /PROT11
- R5 pad 1: OUT3 -> RS485A
- R5 pad 2: Net-(R5-Pad2) -> +3V3
- R50 pad 1: IO15 -> Net-(C20-Pad1)
- R50 pad 2: Net-(Q8-Pad1) -> /PROT13
- R51 pad 1: IO12 -> Net-(C18-Pad1)
- R52 pad 1: IO13 -> Net-(C19-Pad1)
- R53 pad 1: IO14 -> Net-(C20-Pad1)
- R54 pad 1: IO15 -> +3V3
- R54 pad 2: +3V3 -> Net-(R54-Pad2)
- R55 pad 1: /io4_A/S0 -> GND
- R55 pad 2: /io4_A/OUT0 -> Net-(R54-Pad2)
- R56 pad 1: /io4_A/S1 -> /top_hmi/BUZZER
- R56 pad 2: /io4_A/OUT1 -> Net-(Q2-Pad1)
- R57 pad 1: Net-(Q11-Pad1) -> Net-(Q2-Pad3)
- R57 pad 2: /io4_A/OUT2 -> Net-(BZ1-PadN)
- R58 pad 1: Net-(Q12-Pad1) -> GND1
- R58 pad 2: /io4_A/OUT3 -> /top_hmi/SW
- R59 pad 1: GND -> /top_hmi/SW
- R59 pad 2: /io4_A/S0 -> Net-(R59-Pad2)
- R6 pad 1: OUT2 -> GND
- R6 pad 2: Net-(R6-Pad2) -> RS485B
- R60 pad 1: GND -> /top_hmi/SW
- R60 pad 2: /io4_A/S1 -> Net-(R60-Pad2)
- R61 pad 1: GND -> /top_hmi/SW
- R61 pad 2: Net-(Q11-Pad1) -> Net-(R61-Pad2)
- R62 pad 2: Net-(Q12-Pad1) -> CPU13
- R63 pad 1: IO4 -> Net-(R63-Pad1)
- R63 pad 2: /io4_A/S0 -> Net-(R10-Pad2)
- R64 pad 1: IO5 -> Net-(R64-Pad1)
- R64 pad 2: /io4_A/S1 -> +15V
- R65 pad 1: IO6 -> GND
- R65 pad 2: Net-(Q11-Pad1) -> Net-(R64-Pad1)
- R66 pad 1: IO7 -> CPU8
- R66 pad 2: Net-(Q12-Pad1) -> Net-(R66-Pad2)
- R67 pad 1: IO4 -> CPU9
- R67 pad 2: +3V3 -> Net-(R67-Pad2)
- R68 pad 1: IO5 -> CPU10
- R68 pad 2: +3V3 -> Net-(U1-Pad12)
- R69 pad 1: IO6 -> CPU7
- R69 pad 2: +3V3 -> Net-(R69-Pad2)
- R7 pad 1: OUT1 -> GND
- R70 pad 1: IO7 -> CPU6
- R70 pad 2: +3V3 -> Net-(R70-Pad2)
- R71 pad 1: CANL -> CPU5
- R71 pad 2: CANT -> Net-(R71-Pad2)
- R72 pad 1: IO15 -> CPU4
- R72 pad 2: +3V3 -> Net-(R72-Pad2)
- R73 pad 1: CANH -> CPU3
- R74 pad 1: 3V3_ZDIODE -> CPU2
- R74 pad 2: +24V -> Net-(R74-Pad2)
- R75 pad 1: CANH -> CPU1
- R75 pad 2: +3V3 -> Net-(R75-Pad2)
- R76 pad 1: CANL -> CPU0
- R76 pad 2: +3V3 -> Net-(R76-Pad2)
- R77 pad 1: GND -> CPU13
- R77 pad 2: Net-(D1-Pad3) -> Net-(U1-Pad11)
- R78 pad 1: Net-(R78-Pad1) -> CPU12
- R78 pad 2: +3V3 -> Net-(U1-Pad10)
- R79 pad 1: Net-(R79-Pad1) -> CPU11
- R79 pad 2: PROG_EN -> Net-(U1-Pad13)
- R8 pad 1: OUT0 -> Net-(Q1-Pad3)
- R9 pad 1: +3V3 -> BUS_2
- R9 pad 2: /psu/FB -> Net-(R9-Pad2)
- SW2 pad 1: CANL -> unconnected-(SW2-Pad1)
- SW2 pad 2: Net-(R73-Pad2) -> BUS_1
- SW2 pad 3: Net-(SW2-Pad3) -> Net-(R9-Pad2)
- SW3 pad 1: Net-(R79-Pad1) -> /top_hmi/RESET
- SW3 pad 2: GND -> GND1
- SW4 pad 1: IRQ -> +3.3VP
- SW4 pad 2: +5VA -> Net-(R59-Pad2)
- SW5 pad 1: IRQ -> +3.3VP
- SW5 pad 2: Net-(J1-Pad5) -> Net-(R60-Pad2)
- SW6 pad 1: IRQ -> +3.3VP
- SW6 pad 2: GNDA -> Net-(R61-Pad2)
- U1 pad 10: IO6 -> Net-(U1-Pad10)
- U1 pad 11: IO7 -> Net-(U1-Pad11)
- U1 pad 12: IO8 -> Net-(U1-Pad12)
- U1 pad 13: IO9 -> Net-(U1-Pad13)
- U1 pad 14: OUT3 -> IO12
- U1 pad 16: IO10 -> Net-(R67-Pad2)
- U1 pad 17: Net-(U1-Pad17) -> unconnected-(U1-Pad17)
- U1 pad 18: Net-(U1-Pad18) -> unconnected-(U1-Pad18)
- U1 pad 19: Net-(U1-Pad19) -> unconnected-(U1-Pad19)
- U1 pad 20: Net-(U1-Pad20) -> unconnected-(U1-Pad20)
- U1 pad 21: Net-(U1-Pad21) -> unconnected-(U1-Pad21)
- U1 pad 22: Net-(U1-Pad22) -> unconnected-(U1-Pad22)
- U1 pad 23: OUT2 -> Net-(R69-Pad2)
- U1 pad 24: OUT1 -> RS
- U1 pad 25: PROG_IO0 -> BACKLIGHT
- U1 pad 26: IO11 -> Net-(R66-Pad2)
- U1 pad 27: IO12 -> Net-(R70-Pad2)
- U1 pad 28: IO13 -> Net-(R71-Pad2)
- U1 pad 29: OUT0 -> BUS_TX
- U1 pad 30: IO14 -> Net-(R72-Pad2)
- U1 pad 31: IO15 -> Net-(R73-Pad2)
- U1 pad 32: Net-(U1-Pad32) -> unconnected-(U1-Pad32)
- U1 pad 33: CANT -> Net-(R74-Pad2)
- U1 pad 36: CANR -> Net-(R75-Pad2)
- U1 pad 37: IRQ -> Net-(R76-Pad2)
- U1 pad 4: IN0 -> unconnected-(U1-Pad4)
- U1 pad 5: IN1 -> unconnected-(U1-Pad5)
- U1 pad 6: IN2 -> BUS_RX
- U1 pad 7: IN3 -> SW1
- U1 pad 8: IO4 -> SCLK
- U1 pad 9: IO5 -> MOSI
- U10 pad 1: Net-(Q4-Pad1) -> Net-(C23-Pad1)
- U10 pad 3: Net-(Q3-Pad1) -> Net-(R54-Pad2)
- U10 pad 4: /io4_B/S1 -> +24V
- U10 pad 5: 3V3_ZDIODE -> +24V
- U10 pad 6: /io4_B/S0 -> /psu/SW
- U11 pad 1: Net-(Q8-Pad1) -> Net-(R64-Pad1)
- U11 pad 2: GND -> +15V
- U11 pad 3: Net-(Q7-Pad1) -> +24V
- U12 pad 1: Net-(Q12-Pad1) -> 485_RO
- U12 pad 2: GND -> 485_DE
- U12 pad 3: Net-(Q11-Pad1) -> 485_DE
- U12 pad 4: /io4_A/S1 -> 485_DI
- U12 pad 5: 3V3_ZDIODE -> GND
- U12 pad 6: /io4_A/S0 -> RS485A
- U13 pad 1: IO13 -> CPU0
- U13 pad 2: Net-(JP1-Pad2) -> GND
- U13 pad 3: GND -> CPU1
- U13 pad 4: +3V3 -> CPU2
- U13 pad 5: Net-(U13-Pad5) -> +3V0
- U13 pad 6: Net-(U13-Pad6) -> unconnected-(U13-Pad6)
- U14 pad 1: IO13 -> CPU3
- U14 pad 2: Net-(JP1-Pad2) -> GND
- U14 pad 3: GND -> CPU4
- U14 pad 4: Net-(R78-Pad1) -> CPU6
- U14 pad 5: Net-(U14-Pad5) -> +3V0
- U14 pad 6: Net-(U14-Pad6) -> CPU5
- U2 pad 1: +3V3 -> CANT
- U2 pad 2: CANR -> GND
- U2 pad 3: CANT -> +3V3
- U2 pad 4: GND -> CANR
- U2 pad 5: GNDA -> unconnected-(U2-Pad5)
- U2 pad 8: +5VA -> Net-(R7-Pad2)
- U3 pad 1: GND -> /ULN0
- U3 pad 10: IO15 -> /CONN6
- U3 pad 2: Net-(U3-Pad2) -> /ULN1
- U3 pad 3: GND -> /ULN2
- U3 pad 4: Net-(R83-Pad2) -> /ULN3
- U3 pad 5: Net-(R84-Pad2) -> /ULN4
- U3 pad 6: Net-(R81-Pad2) -> /ULN5
- U3 pad 7: Net-(R82-Pad2) -> /ULN6
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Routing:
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- added copper zone on B.Cu, net GND1
- added copper zone on F.Cu, net GND1
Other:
- board size 90 x 58.5 mm -> 90 x 74.6 mm
- net class Default removed
- net class HigherVoltage removed
- board text removed: "CH CL CL CH"
- board text removed: "GN 24"
- board text removed: "IN0-3 IO4-7"
- board text removed: "IO8...15"
- board text removed: "OUT3-0"
- board text removed: "RED: POWER GREEN:INFO"
